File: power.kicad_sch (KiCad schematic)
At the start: 58 parts, among them U90 STWD100NYWY3F, U92 MAX4495ALAUT, U93 MAX4495ALAUT, U94 MAX4495ALAUT, U95 STWD100NYWY3F, U96 TPSM828302ARDSR, U97 LP3962EMP-3.3/NOPB, U98 MP5073GG-P

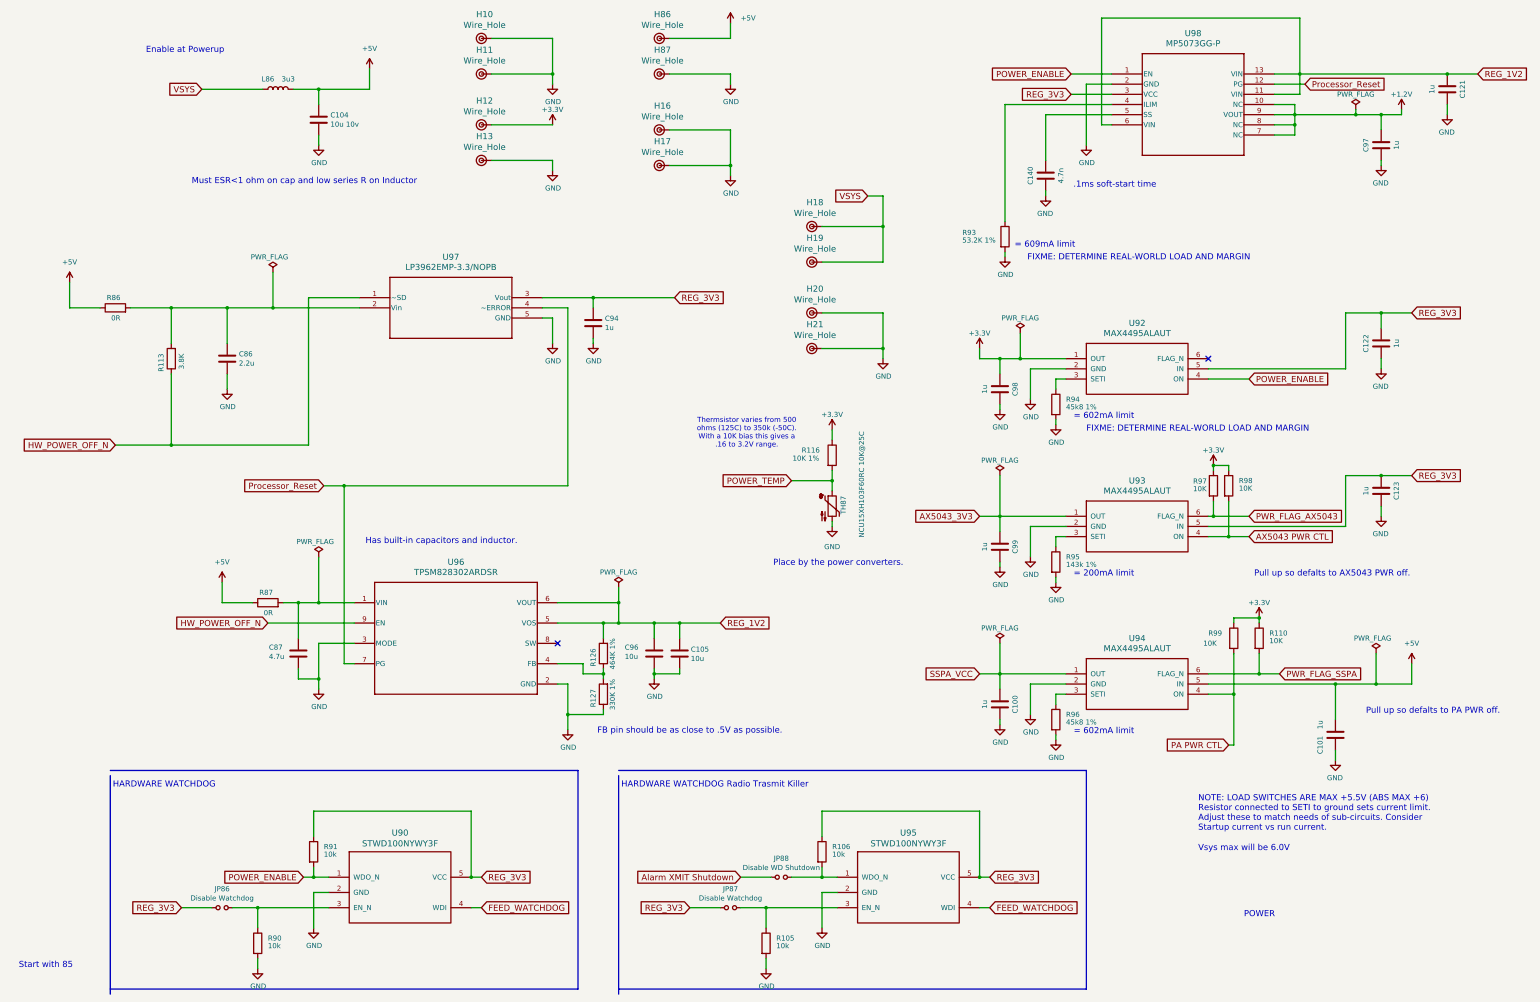
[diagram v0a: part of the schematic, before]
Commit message: Re-annotate all parts
And get rid of the per-sheet annotation remarks.

Signed-off-by: Corey Minyard <corey@minyard.net>
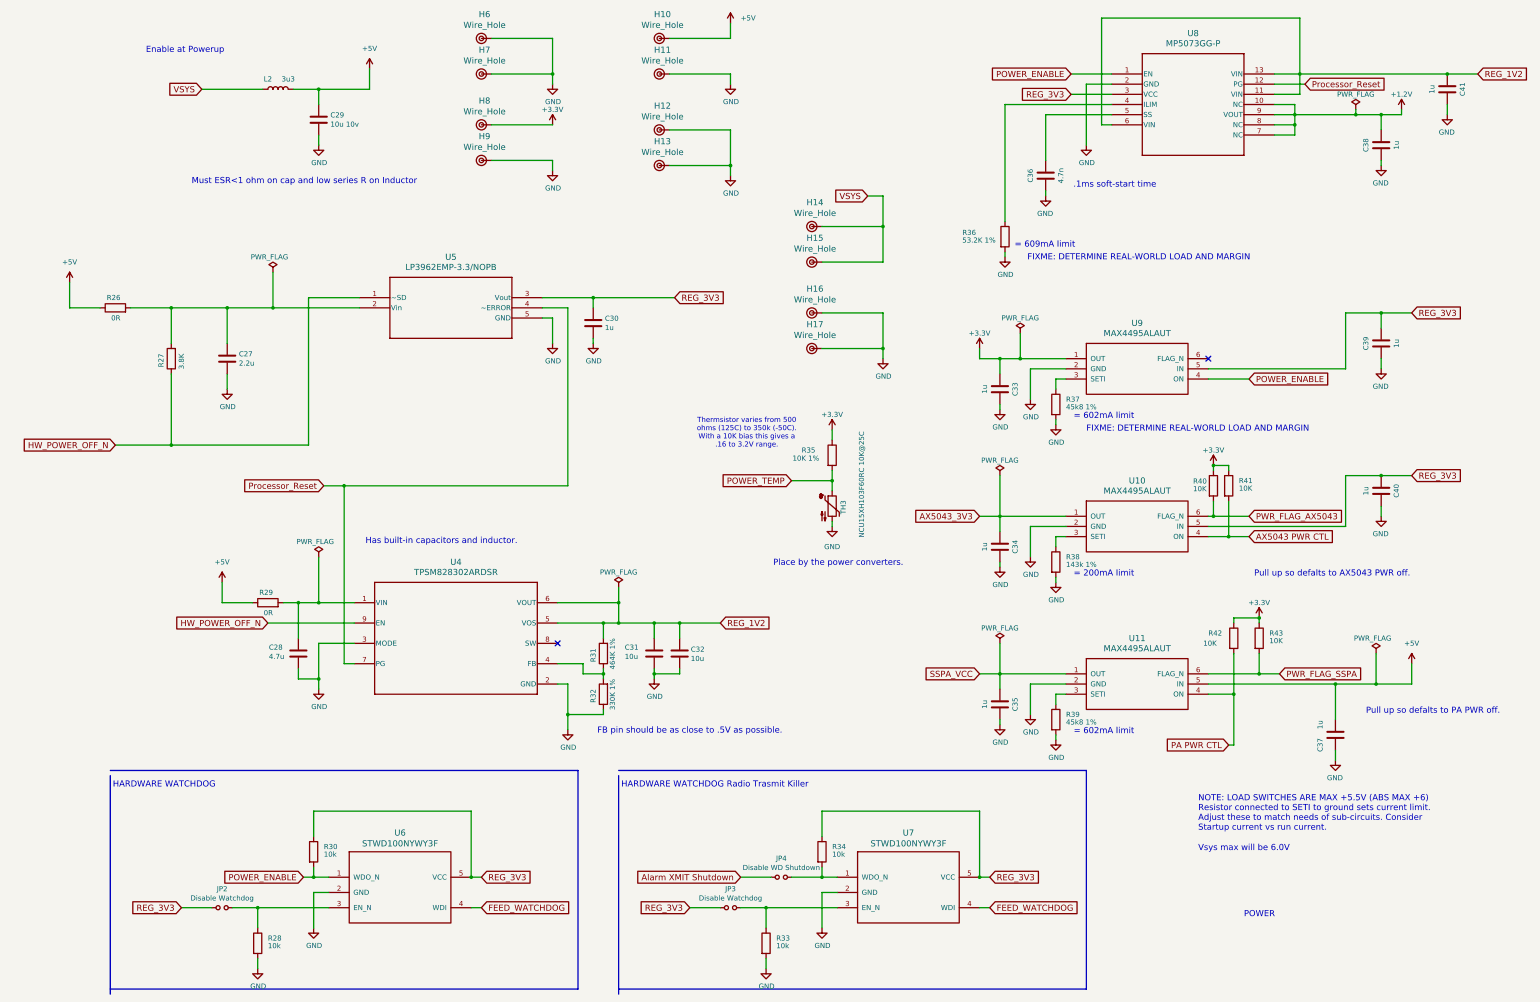
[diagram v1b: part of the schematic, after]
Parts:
- renumbered C86 to C27, C87 to C28, C104 to C29, C94 to C30, C96 to C31, C105 to C32, C98 to C33, C99 to C34, C100 to C35, C140 to C36, C101 to C37, C97 to C38, C122 to C39, C123 to C40, C121 to C41, H86 to H10, H87 to H11, H16 to H12, H17 to H13, H18 to H14, H19 to H15, H20 to H16, H21 to H17, H10 to H6, H11 to H7, H12 to H8, H13 to H9, JP86 to JP2, JP87 to JP3, JP88 to JP4, L86 to L2, R86 to R26, R113 to R27, R90 to R28, R87 to R29, R91 to R30, R126 to R31, R127 to R32, R105 to R33, R106 to R34, R116 to R35, R93 to R36, R94 to R37, R95 to R38, R96 to R39, R97 to R40, R98 to R41, R99 to R42, R110 to R43, TH87 to TH3, U93 to U10, U94 to U11, U96 to U4, U97 to U5, U90 to U6, U95 to U7, U98 to U8, U92 to U9
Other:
- note removed: "Start with 85"

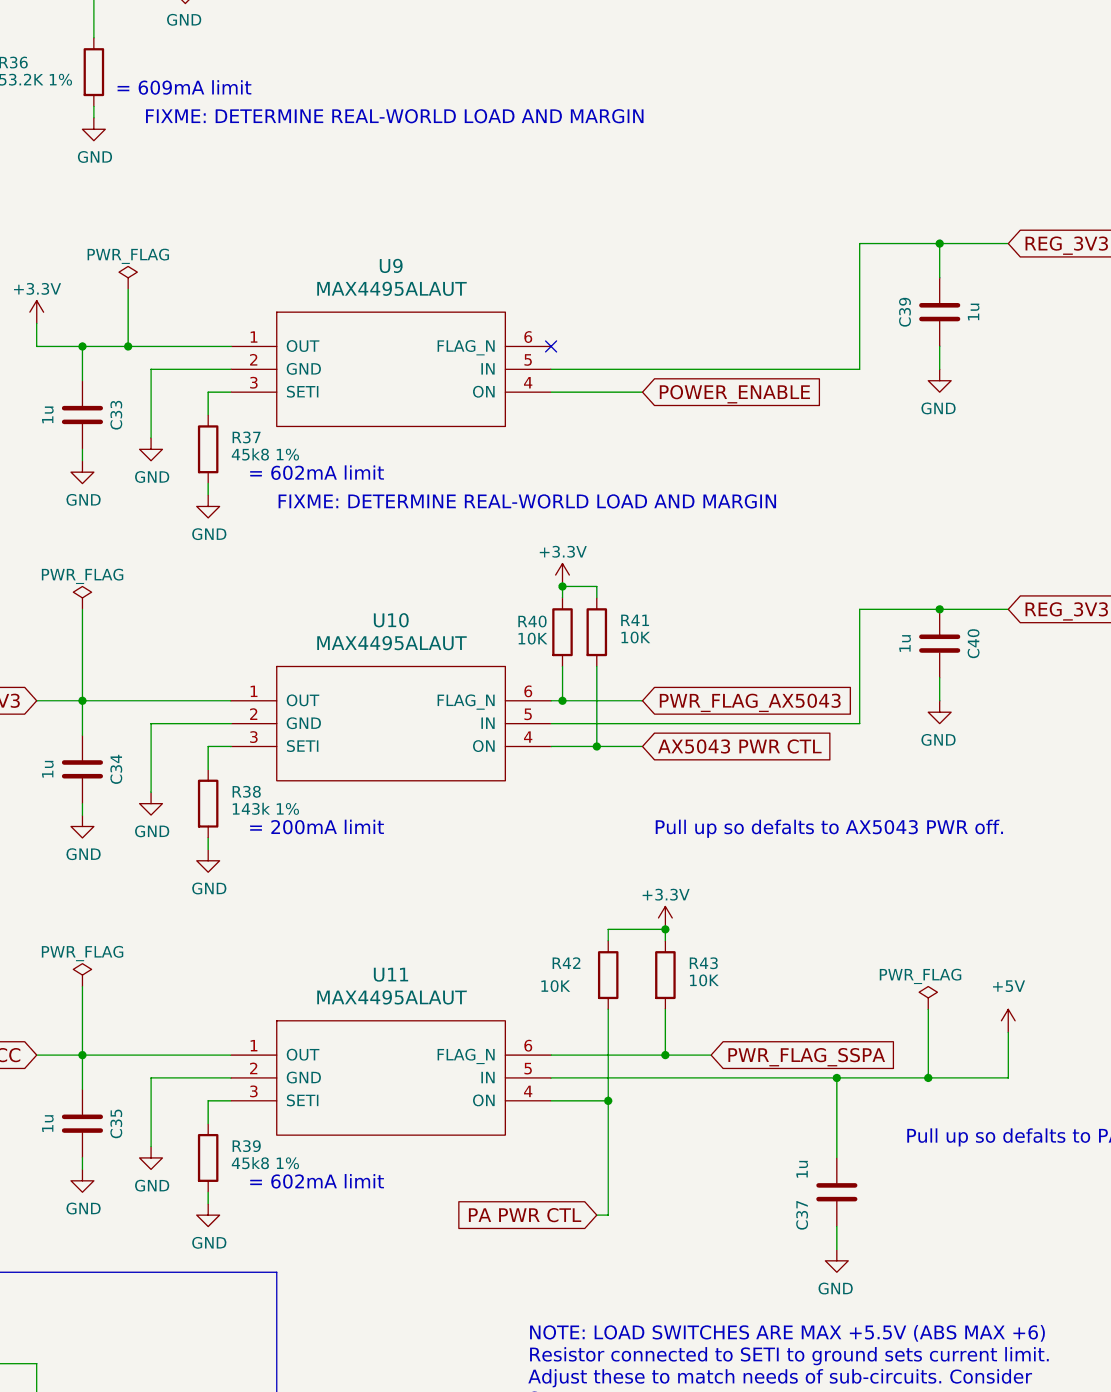
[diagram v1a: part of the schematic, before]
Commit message: More notes, added a pullup on LNA_ENABLE_N
Signed-off-by: Corey Minyard <corey@minyard.net>
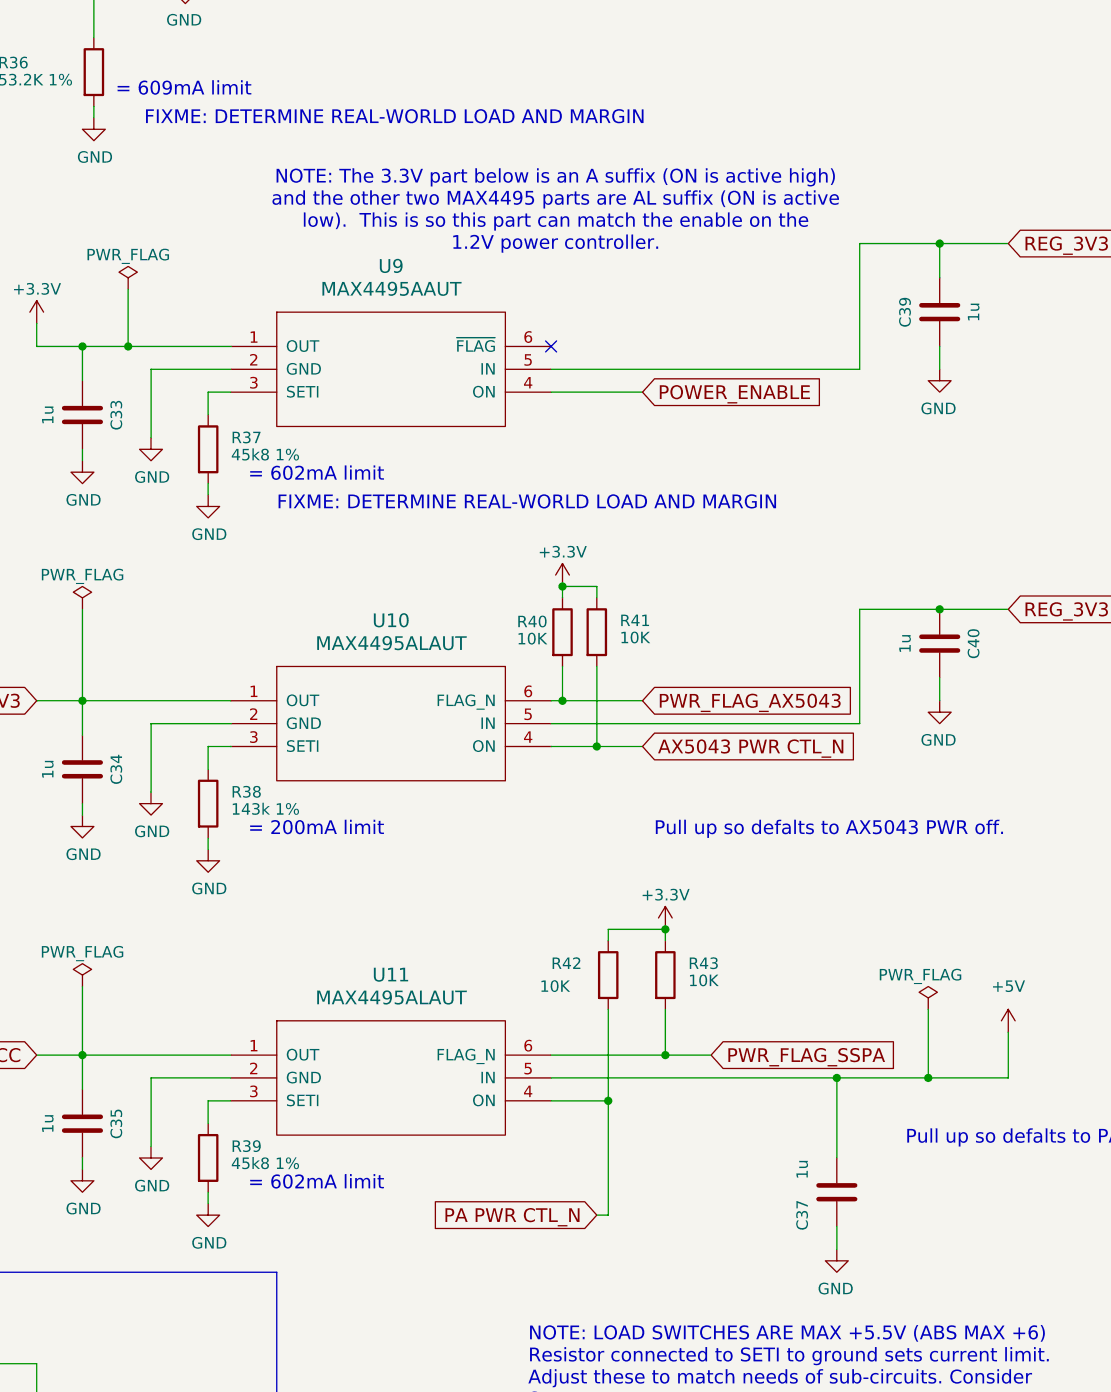
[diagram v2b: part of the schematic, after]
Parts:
- U9: value MAX4495ALAUT -> MAX4495AAUT; symbol PACSAT_ICs:MAX4995ALAUT -> PACSAT_ICs:MAX4995AAUT
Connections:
- net AX5043 PWR CTL renamed AX5043 PWR CTL_N
- net PA PWR CTL renamed PA PWR CTL_N
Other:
- note added: "NOTE: The 3.3V part below is an A suffix (ON is active high) and the other two MAX4495 parts are AL suffix (ON is active low). This is so this part can match the enable on the 1.2V power controller."
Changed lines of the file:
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@@
 		)
 	)
+	(text "NOTE: The 3.3V part below is an A suffix (ON is active high)\nand the other two MAX4495 parts are AL suffix (ON is active\nlow).  This is so this part can match the enable on the\n1.2V power controller."
+		(exclude_from_sim no)
+		(at 325.628 90.424 0)
+		(effects
+			(font
+				(size 1.524 1.524)
+			)
+		)
+	)
 	(text "Enable at Powerup"
 		(exclude_from_sim no)
@@
 		)
 	)
-	(global_label "AX5043 PWR CTL"
+	(global_label "AX5043 PWR CTL_N"
 		(shape input)
 		(at 335.28 149.86 0)
@@
 		)
 		(property "Intersheetrefs" "${INTERSHEET_REFS}"
-			(at 357.6708 149.86 0)
+			(at 360.4285 149.86 0)
 			(effects
 				(font
@@
 		)
 	)
-	(global_label "PA PWR CTL"
+	(global_label "PA PWR CTL_N"
 		(shape input)
 		(at 330.2 201.93 180)
@@
 		)
 		(property "Intersheetrefs" "${INTERSHEET_REFS}"
-			(at 313.5422 201.93 0)
+			(at 310.7845 201.93 0)
 			(effects
 				(font
@@
 	)
 	(symbol
-		(lib_id "PACSAT_ICs:MAX4995ALAUT")
+		(lib_id "PACSAT_ICs:MAX4995AAUT")
 		(at 307.34 107.95 0)
 		(unit 1)
@@
 			)
 		)
-		(property "Value" "MAX4495ALAUT"
+		(property "Value" "MAX4495AAUT"
 			(at 307.34 99.06 0)
 			(effects

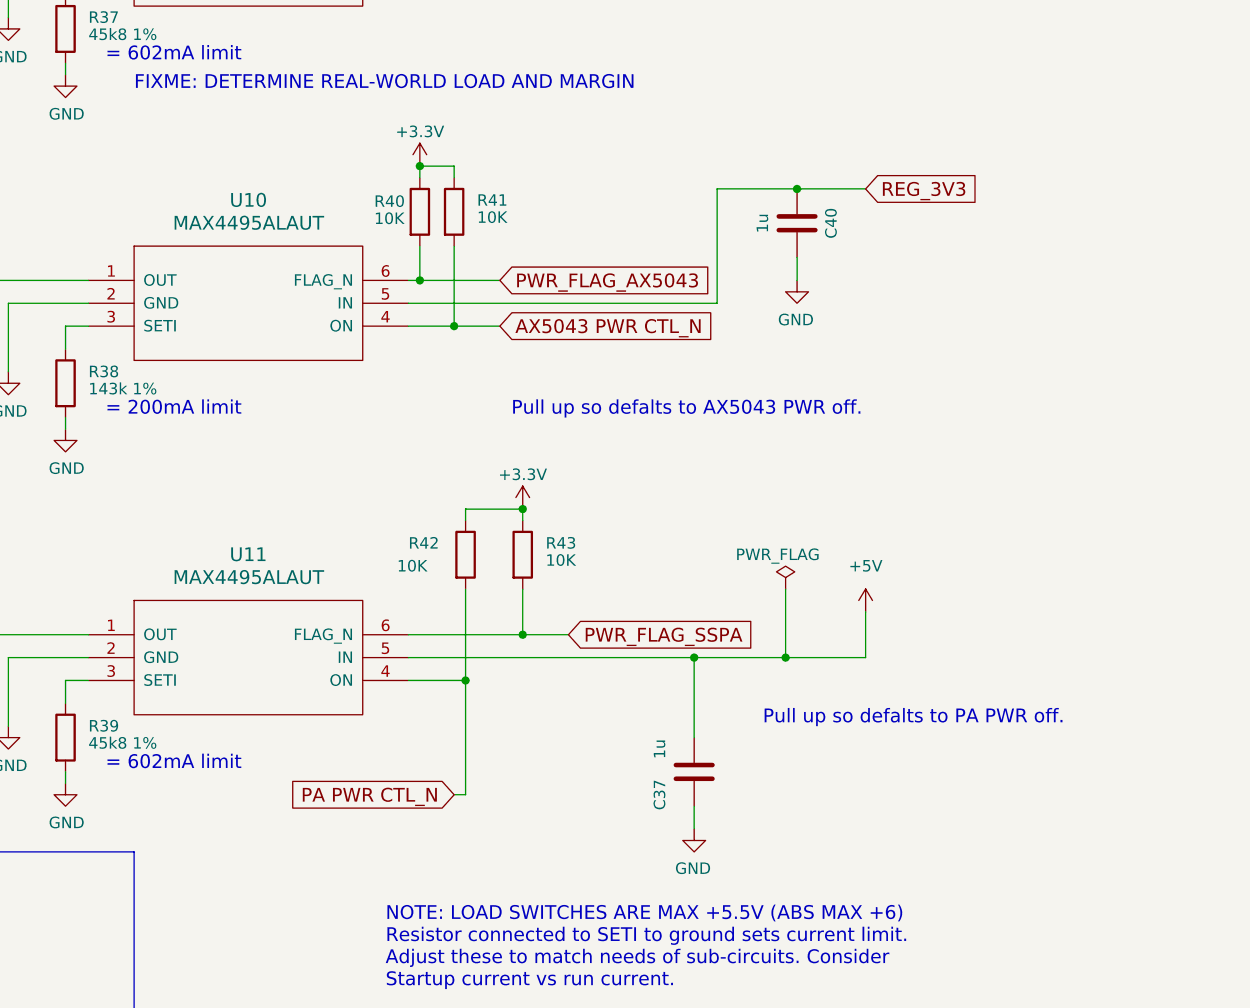
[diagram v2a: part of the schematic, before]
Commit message: Rework AX5043 and PA power enables
The way they were wasn't going to work, make the enables active high.

Signed-off-by: Corey Minyard <corey@minyard.net>
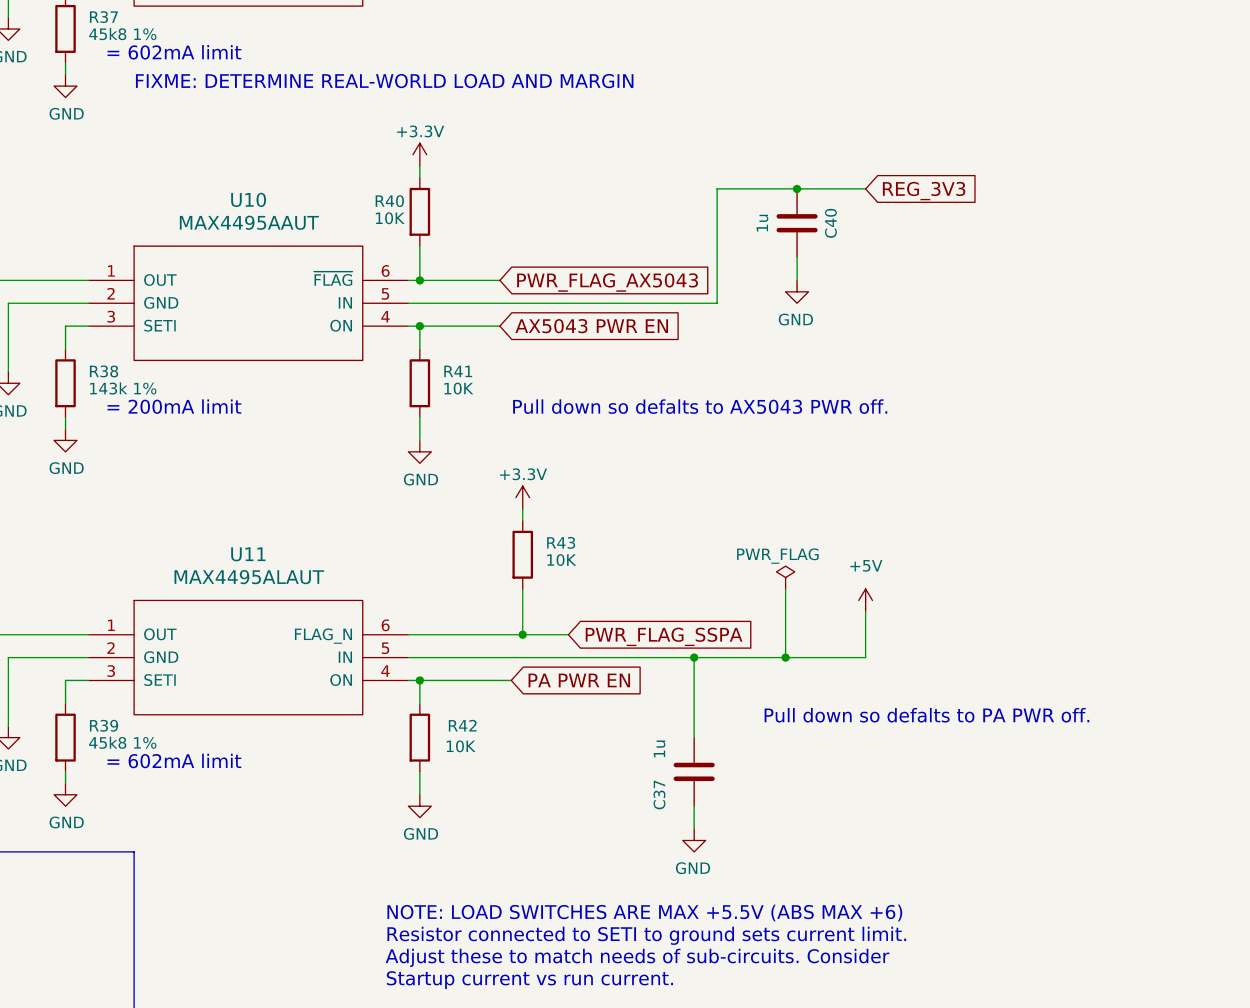
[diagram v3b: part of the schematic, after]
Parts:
- U10: value MAX4495ALAUT -> MAX4495AAUT; symbol PACSAT_ICs:MAX4995ALAUT -> PACSAT_ICs:MAX4995AAUT
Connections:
- net +3.3V: no longer R41.1, R42.1
- net GND: now also R41.2, R42.2
- net AX5043 PWR CTL_N renamed AX5043 PWR EN
- net AX5043 PWR EN: now also R41.1; no longer R41.2
- net PA PWR CTL_N renamed PA PWR EN
- net PA PWR EN: now also R42.1; no longer R42.2
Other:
- note added: "Pull down so defalts to AX5043 PWR off."
- note added: "Pull down so defalts to PA PWR off."
- note removed: "Pull up so defalts to AX5043 PWR off."
- note removed: "Pull up so defalts to PA PWR off."
- moved on the sheet: R41, R42
